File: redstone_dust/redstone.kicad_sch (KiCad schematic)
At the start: 72 parts, among them J1 1x4_Pogo, J2 1x4_Pogo, J3 1x4_Pogo, J4 1x4_Pogo, J5 1x4_Pogo, J6 1x4_Pogo, J7 1x4_Pogo, J8 1x4_Pogo, J9 2.54mm_ProgrammingPin, Q1 BC108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

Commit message: add some symbol footprints
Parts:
- D1, D10, D11, D12, D13, D14, D15, D16, D2, D3, D4, D5, D6, D7, D8, D9: footprint (none) -> SamacSys_Parts:LEDC1608X115N
- J9: footprint (none) -> Connector_PinSocket_2.54mm:PinSocket_1x04_P2.54mm_Vertical
- R1, R10, R11, R12, R13, R14, R15, R16, R17, R18, R19, R2, R20, R21, R3, R4, R5, R6, R7, R8, R9: footprint (none) -> Resistor_THT:R_Axial_DIN0204_L3.6mm_D1.6mm_P5.08mm_Horizontal
- SW1: footprint (none) -> Button_Switch_THT:SW_TH_Tactile_Omron_B3F-100x
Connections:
- net GND: now also J9.4 (Pin_4); no longer J9.1 (Pin_1)
- net at J9.2 (Pin_2): now also U1.24 (SWCLK); no longer U1.25 (SWD)
- net at J9.3 (Pin_3): now also U1.25 (SWD); no longer U1.24 (SWCLK)
- net at SW1.2 (B), U1.26 (RUN): now also J9.1 (Pin_1); no longer J9.4 (Pin_4)
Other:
- moved on the sheet: J9
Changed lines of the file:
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@@
 	)
 	(no_connect
-		(at 41.91 144.78)
+		(at 41.91 162.56)
 	)
 	(no_connect
@@
 			(width 0)
 			(type default)
+			(color 0 0 0 1)
 		)
 	)
@@
 			(width 0)
 			(type default)
+			(color 0 0 0 1)
 		)
 	)
@@
 	(wire
 		(pts
-			(xy 31.75 173.99) (xy 31.75 21.59)
+			(xy 22.86 173.99) (xy 22.86 21.59)
 		)
 		(stroke
@@
 	(wire
 		(pts
-			(xy 31.75 21.59) (xy 82.55 21.59)
+			(xy 22.86 21.59) (xy 82.55 21.59)
 		)
 		(stroke
@@
 	(wire
 		(pts
-			(xy 31.75 173.99) (xy 62.23 173.99)
+			(xy 22.86 173.99) (xy 62.23 173.99)
 		)
 		(stroke
@@
 			(width 0)
 			(type default)
+			(color 0 0 0 1)
 		)
 	)
@@
 			)
 		)
-		(property "Footprint" ""
+		(property "Footprint" "Resistor_THT:R_Axial_DIN0204_L3.6mm_D1.6mm_P5.08mm_Horizontal"
 			(at 207.01 35.56 0)
 			(effects
@@
 	(symbol
 		(lib_id "Connector_Generic_MountingPin:Conn_01x04_MountingPin")
-		(at 41.91 154.94 180)
+		(at 41.91 152.4 0)
+		(mirror y)
 		(unit 1)
 		(exclude_from_sim no)
@@
 		(on_board yes)
 		(dnp no)
-		(fields_autoplaced yes)
 		(property "Reference" "J9"
-			(at 39.37 152.0443 0)
+			(at 39.37 155.2957 0)
 			(effects
 				(font
@@
 		)
 		(property "Value" "2.54mm_ProgrammingPin"
-			(at 39.37 154.5843 0)
+			(at 39.37 152.7557 0)
 			(effects
 				(font
@@
 			)
 		)
-		(property "Footprint" ""
-			(at 41.91 154.94 0)
+		(property "Footprint" "Connector_PinSocket_2.54mm:PinSocket_1x04_P2.54mm_Vertical"
+			(at 41.91 152.4 0)
 			(effects
 				(font
@@
 		)
 		(property "Datasheet" "~"
-			(at 41.91 154.94 0)
+			(at 41.91 152.4 0)
 			(effects
 				(font
@@
 		)
 		(property "Description" "Generic connectable mounting pin connector, single row, 01x04, script generated (kicad-library-utils/schlib/autogen/connector/)"
-			(at 41.91 154.94 0)
+			(at 41.91 152.4 0)
 			(effects
 				(font
@@
 			)
 		)
-		(property "Footprint" ""
+		(property "Footprint" "SamacSys_Parts:LEDC1608X115N"
 			(at 207.01 25.4 0)
 			(effects
@@
 			)
 		)
-		(property "Footprint" ""
+		(property "Footprint" "Resistor_THT:R_Axial_DIN0204_L3.6mm_D1.6mm_P5.08mm_Horizontal"
 			(at 168.91 50.8 0)
 			(effects
@@
 			)
 		)
-		(property "Footprint" ""
+		(property "Footprint" "Resistor_THT:R_Axial_DIN0204_L3.6mm_D1.6mm_P5.08mm_Horizontal"
 			(at 217.17 52.07 0)
 			(effects
@@
 			)
 		)
-		(property "Footprint" ""
+		(property "Footprint" "SamacSys_Parts:LEDC1608X115N"
 			(at 196.85 25.4 0)
 			(effects
@@
 			)
 		)
-		(property "Footprint" ""
+		(property "Footprint" "Resistor_THT:R_Axial_DIN0204_L3.6mm_D1.6mm_P5.08mm_Horizontal"
 			(at 217.17 19.05 0)
 			(effects
@@
 			)
 		)
-		(property "Footprint" ""
+		(property "Footprint" "Resistor_THT:R_Axial_DIN0204_L3.6mm_D1.6mm_P5.08mm_Horizontal"
 			(at 207.01 19.05 0)
 			(effects
@@
 			)
 		)
-		(property "Footprint" ""
+		(property "Footprint" "Resistor_THT:R_Axial_DIN0204_L3.6mm_D1.6mm_P5.08mm_Horizontal"
 			(at 196.85 52.07 0)
 			(effects
@@
 			)
 		)
-		(property "Footprint" ""
+		(property "Footprint" "Resistor_THT:R_Axial_DIN0204_L3.6mm_D1.6mm_P5.08mm_Horizontal"
 			(at 171.45 62.23 0)
 			(effects
@@
 			)
 		)
-		(property "Footprint" ""
+		(property "Footprint" "Resistor_THT:R_Axial_DIN0204_L3.6mm_D1.6mm_P5.08mm_Horizontal"
 			(at 164.338 21.59 90)
 			(effects
@@
 			)
 		)
-		(property "Footprint" ""
+		(property "Footprint" "Resistor_THT:R_Axial_DIN0204_L3.6mm_D1.6mm_P5.08mm_Horizontal"
 			(at 196.85 68.58 0)
 			(effects
@@
 			)
 		)
-		(property "Footprint" ""
+		(property "Footprint" "SamacSys_Parts:LEDC1608X115N"
 			(at 196.85 41.91 0)
 			(effects
@@
 			)
 		)
-		(property "Footprint" ""
+		(property "Footprint" "SamacSys_Parts:LEDC1608X115N"
 			(at 186.69 41.91 0)
 			(effects
@@
 			)
 		)
-		(property "Footprint" ""
+		(property "Footprint" "SamacSys_Parts:LEDC1608X115N"
 			(at 207.01 74.93 0)
 			(effects
@@
 			)
 		)
-		(property "Footprint" ""
+		(property "Footprint" "Resistor_THT:R_Axial_DIN0204_L3.6mm_D1.6mm_P5.08mm_Horizontal"
 			(at 217.17 35.56 0)
 			(effects
@@
 			)
 		)
-		(property "Footprint" ""
+		(property "Footprint" "SamacSys_Parts:LEDC1608X115N"
 			(at 186.69 25.4 0)
 			(effects
@@
 			)
 		)
-		(property "Footprint" ""
+		(property "Footprint" "SamacSys_Parts:LEDC1608X115N"
 			(at 207.01 41.91 0)
 			(effects
@@
 			)
 		)
-		(property "Footprint" ""
+		(property "Footprint" "SamacSys_Parts:LEDC1608X115N"
 			(at 217.17 25.4 0)
 			(effects
@@
 			)
 		)
-		(property "Footprint" ""
+		(property "Footprint" "Resistor_THT:R_Axial_DIN0204_L3.6mm_D1.6mm_P5.08mm_Horizontal"
 			(at 196.85 35.56 0)
 			(effects
@@
 			)
 		)
-		(property "Footprint" ""
+		(property "Footprint" "SamacSys_Parts:LEDC1608X115N"
 			(at 186.69 74.93 0)
 			(effects
@@
 			)
 		)
-		(property "Footprint" ""
+		(property "Footprint" "SamacSys_Parts:LEDC1608X115N"
 			(at 186.69 58.42 0)
 			(effects
@@
 			)
 		)
-		(property "Footprint" ""
+		(property "Footprint" "Resistor_THT:R_Axial_DIN0204_L3.6mm_D1.6mm_P5.08mm_Horizontal"
 			(at 173.99 77.47 0)
 			(effects
@@
 			)
 		)
-		(property "Footprint" ""
+		(property "Footprint" "SamacSys_Parts:LEDC1608X115N"
 			(at 217.17 58.42 0)
 			(effects
@@
 			)
 		)
-		(property "Footprint" ""
+		(property "Footprint" "SamacSys_Parts:LEDC1608X115N"
 			(at 207.01 58.42 0)
 			(effects
@@
 			)
 		)
-		(property "Footprint" ""
+		(property "Footprint" "SamacSys_Parts:LEDC1608X115N"
 			(at 196.85 74.93 0)
 			(effects
@@
 			)
 		)
-		(property "Footprint" ""
+		(property "Footprint" "SamacSys_Parts:LEDC1608X115N"
 			(at 217.17 74.93 0)
 			(effects
@@
 			)
 		)
-		(property "Footprint" ""
+		(property "Footprint" "Resistor_THT:R_Axial_DIN0204_L3.6mm_D1.6mm_P5.08mm_Horizontal"
 			(at 196.85 19.05 0)
 			(effects
@@
 			)
 		)
-		(property "Footprint" ""
+		(property "Footprint" "Resistor_THT:R_Axial_DIN0204_L3.6mm_D1.6mm_P5.08mm_Horizontal"
 			(at 186.69 68.58 0)
 			(effects
@@
 			)
 		)
-		(property "Footprint" ""
+		(property "Footprint" "Resistor_THT:R_Axial_DIN0204_L3.6mm_D1.6mm_P5.08mm_Horizontal"
 			(at 181.61 90.17 0)
 			(effects
@@
 			)
 		)
-		(property "Footprint" ""
+		(property "Footprint" "Resistor_THT:R_Axial_DIN0204_L3.6mm_D1.6mm_P5.08mm_Horizontal"
 			(at 186.69 35.56 0)
 			(effects
@@
 			)
 		)
-		(property "Footprint" ""
+		(property "Footprint" "SamacSys_Parts:LEDC1608X115N"
 			(at 217.17 41.91 0)
 			(effects
@@
 			)
 		)
-		(property "Footprint" ""
+		(property "Footprint" "Resistor_THT:R_Axial_DIN0204_L3.6mm_D1.6mm_P5.08mm_Horizontal"
 			(at 207.01 52.07 0)
 			(effects
@@
 			)
 		)
-		(property "Footprint" ""
+		(property "Footprint" "Resistor_THT:R_Axial_DIN0204_L3.6mm_D1.6mm_P5.08mm_Horizontal"
 			(at 186.69 52.07 0)
 			(effects
@@
 			)
 		)
-		(property "Footprint" ""
+		(property "Footprint" "Resistor_THT:R_Axial_DIN0204_L3.6mm_D1.6mm_P5.08mm_Horizontal"
 			(at 207.01 68.58 0)
 			(effects
@@
 			)
 		)
-		(property "Footprint" ""
+		(property "Footprint" "Resistor_THT:R_Axial_DIN0204_L3.6mm_D1.6mm_P5.08mm_Horizontal"
 			(at 217.17 68.58 0)
 			(effects
@@
 			)
 		)
-		(property "Footprint" ""
+		(property "Footprint" "Resistor_THT:R_Axial_DIN0204_L3.6mm_D1.6mm_P5.08mm_Horizontal"
 			(at 186.69 19.05 0)
 			(effects
@@
 			)
 		)
-		(property "Footprint" ""
+		(property "Footprint" "SamacSys_Parts:LEDC1608X115N"
 			(at 196.85 58.42 0)
 			(effects
@@
 			)
 		)
-		(property "Footprint" ""
+		(property "Footprint" "Button_Switch_THT:SW_TH_Tactile_Omron_B3F-100x"
 			(at 53.34 62.23 0)
 			(effects

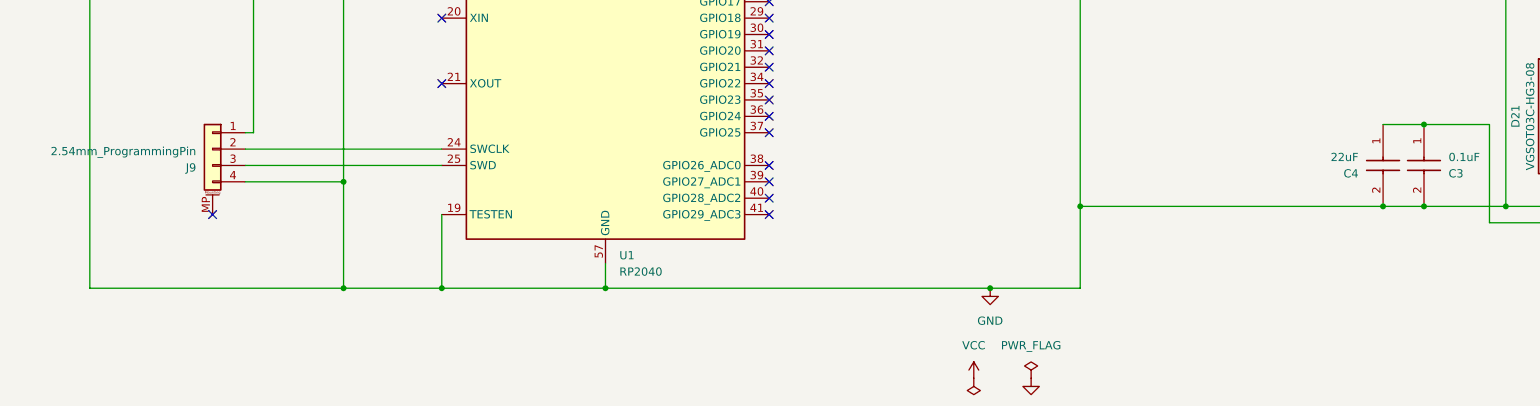
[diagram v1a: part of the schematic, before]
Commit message: add footprint for pogo pins
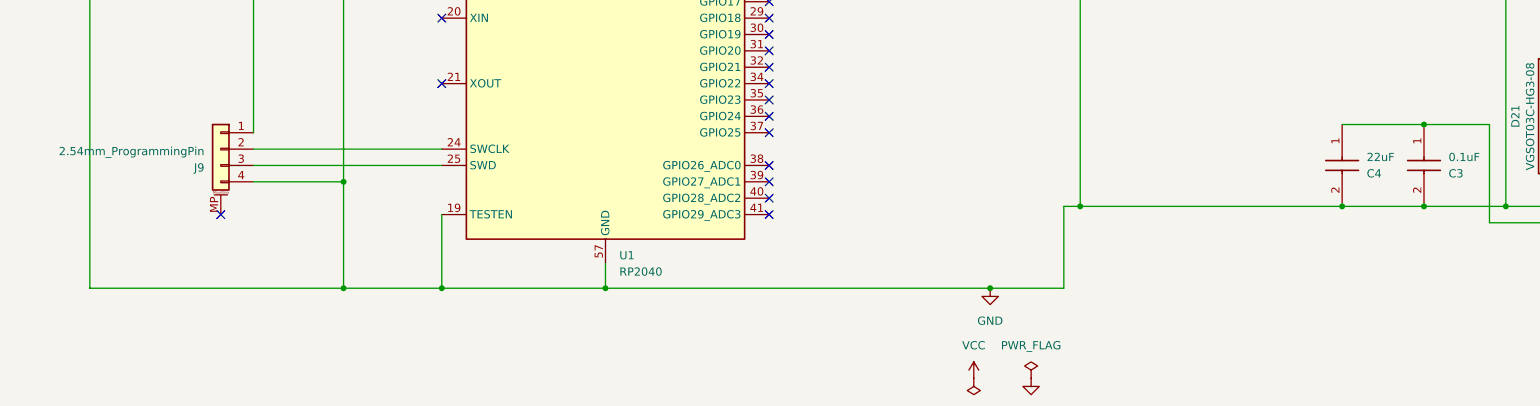
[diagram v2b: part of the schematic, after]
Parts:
- J1, J2, J3, J4, J5, J6, J7, J8: footprint (none) -> Connector_PinSocket_2.54mm:PinSocket_1x04_P2.54mm_Vertical
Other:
- moved on the sheet: C4, J9
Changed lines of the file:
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@@
 	)
 	(junction
-		(at 223.52 161.29)
-		(diameter 0)
-		(color 0 0 0 1)
-	)
-	(junction
 		(at 262.89 21.59)
 		(diameter 0)
@@
 	)
 	(junction
+		(at 217.17 161.29)
+		(diameter 0)
+		(color 0 0 0 0)
+	)
+	(junction
 		(at 260.35 62.23)
 		(diameter 0)
@@
 	)
 	(no_connect
-		(at 41.91 162.56)
+		(at 43.18 162.56)
 	)
 	(no_connect
@@
 	(wire
 		(pts
+			(xy 217.17 161.29) (xy 229.87 161.29)
+		)
+		(stroke
+			(width 0)
+			(type default)
+			(color 0 0 0 1)
+		)
+	)
+	(wire
+		(pts
 			(xy 260.35 118.11) (xy 260.35 128.27)
 		)
@@
 	(wire
 		(pts
-			(xy 46.99 154.94) (xy 77.47 154.94)
+			(xy 48.26 154.94) (xy 77.47 154.94)
 		)
 		(stroke
@@
 	(wire
 		(pts
-			(xy 46.99 149.86) (xy 48.26 149.86)
+			(xy 226.06 16.51) (xy 226.06 33.02)
 		)
 		(stroke
 			(width 0)
 			(type default)
+			(color 255 0 0 1)
 		)
 	)
 	(wire
 		(pts
-			(xy 226.06 16.51) (xy 226.06 33.02)
+			(xy 265.43 100.33) (xy 265.43 113.03)
 		)
 		(stroke
 			(width 0)
 			(type default)
-			(color 255 0 0 1)
+			(color 0 194 194 1)
 		)
 	)
 	(wire
 		(pts
-			(xy 265.43 100.33) (xy 265.43 113.03)
+			(xy 173.99 161.29) (xy 176.53 161.29)
 		)
 		(stroke
 			(width 0)
 			(type default)
-			(color 0 194 194 1)
+			(color 0 0 0 1)
 		)
 	)
@@
 	(wire
 		(pts
-			(xy 176.53 173.99) (xy 176.53 161.29)
+			(xy 173.99 173.99) (xy 173.99 161.29)
 		)
 		(stroke
@@
 	(wire
 		(pts
-			(xy 223.52 148.59) (xy 229.87 148.59)
-		)
-		(stroke
-			(width 0)
-			(type default)
-			(color 194 0 0 1)
-		)
-	)
-	(wire
-		(pts
 			(xy 176.53 63.5) (xy 176.53 80.01)
 		)
@@
 	(wire
 		(pts
-			(xy 176.53 161.29) (xy 223.52 161.29)
+			(xy 176.53 161.29) (xy 217.17 161.29)
 		)
 		(stroke
@@
 	(wire
 		(pts
-			(xy 46.99 152.4) (xy 77.47 152.4)
+			(xy 48.26 152.4) (xy 77.47 152.4)
 		)
 		(stroke
@@
 	(wire
 		(pts
-			(xy 223.52 161.29) (xy 229.87 161.29)
-		)
-		(stroke
-			(width 0)
-			(type default)
-			(color 0 0 0 1)
-		)
-	)
-	(wire
-		(pts
 			(xy 72.39 109.22) (xy 77.47 109.22)
 		)
@@
 	(wire
 		(pts
-			(xy 162.56 173.99) (xy 176.53 173.99)
+			(xy 162.56 173.99) (xy 173.99 173.99)
 		)
 		(stroke
@@
 	(wire
 		(pts
+			(xy 217.17 148.59) (xy 229.87 148.59)
+		)
+		(stroke
+			(width 0)
+			(type default)
+			(color 194 0 0 1)
+		)
+	)
+	(wire
+		(pts
 			(xy 162.56 25.4) (xy 162.56 36.83)
 		)
@@
 	(wire
 		(pts
-			(xy 46.99 157.48) (xy 62.23 157.48)
+			(xy 48.26 157.48) (xy 62.23 157.48)
 		)
 		(stroke
@@
 	(symbol
 		(lib_id "Connector_Generic_MountingPin:Conn_01x04_MountingPin")
-		(at 41.91 152.4 0)
+		(at 43.18 152.4 0)
 		(mirror y)
 		(unit 1)
@@
 		(dnp no)
 		(property "Reference" "J9"
-			(at 39.37 155.2957 0)
+			(at 40.64 155.2957 0)
 			(effects
 				(font
@@
 		)
 		(property "Value" "2.54mm_ProgrammingPin"
-			(at 39.37 152.7557 0)
+			(at 40.64 152.7557 0)
 			(effects
 				(font
@@
 		)
 		(property "Footprint" "Connector_PinSocket_2.54mm:PinSocket_1x04_P2.54mm_Vertical"
-			(at 41.91 152.4 0)
+			(at 43.18 152.4 0)
 			(effects
 				(font
@@
 		)
 		(property "Datasheet" "~"
-			(at 41.91 152.4 0)
+			(at 43.18 152.4 0)
 			(effects
 				(font
@@
 		)
 		(property "Description" "Generic connectable mounting pin connector, single row, 01x04, script generated (kicad-library-utils/schlib/autogen/connector/)"
-			(at 41.91 152.4 0)
+			(at 43.18 152.4 0)
 			(effects
 				(font
@@
 	(symbol
 		(lib_id "SamacSys_Parts:GRM188C81A226ME01D")
-		(at 223.52 148.59 270)
+		(at 217.17 148.59 90)
+		(mirror x)
 		(unit 1)
 		(exclude_from_sim no)
@@
 		(dnp no)
 		(property "Reference" "C4"
-			(at 219.71 156.2101 90)
+			(at 220.98 156.2101 90)
 			(effects
 				(font
@@
 		)
 		(property "Value" "22uF"
-			(at 219.71 153.6701 90)
+			(at 220.98 153.6701 90)
 			(effects
 				(font
@@
 		)
 		(property "Footprint" "GRM18x"
-			(at 127.33 157.48 0)
+			(at 313.36 157.48 0)
 			(effects
 				(font
@@
 		)
 		(property "Datasheet" "https://search.murata.co.jp/Ceramy/image/img/A01X/G101/ENG/GRM188C81A226ME01-01A.pdf"
-			(at 27.33 157.48 0)
+			(at 413.36 157.48 0)
 			(effects
 				(font
@@
 		)
 		(property "Description" "MLCC, 0603"
-			(at 223.52 148.59 0)
+			(at 217.17 148.59 0)
 			(effects
 				(font
@@
 		)
 		(property "Height" "0.9"
-			(at -172.67 157.48 0)
+			(at 613.36 157.48 0)
 			(effects
 				(font
@@
 		)
 		(property "Manufacturer_Name" "Murata Electronics"
-			(at -272.67 157.48 0)
+			(at 713.36 157.48 0)
 			(effects
 				(font
@@
 		)
 		(property "Manufacturer_Part_Number" "GRM188C81A226ME01D"
-			(at -372.67 157.48 0)
+			(at 813.36 157.48 0)
 			(effects
 				(font
@@
 		)
 		(property "Mouser Part Number" ""
-			(at -472.67 157.48 0)
+			(at 913.36 157.48 0)
 			(effects
 				(font
@@
 		)
 		(property "Mouser Price/Stock" ""
-			(at -572.67 157.48 0)
+			(at 1013.36 157.48 0)
 			(effects
 				(font
@@
 		)
 		(property "Arrow Part Number" ""
-			(at -672.67 157.48 0)
+			(at 1113.36 157.48 0)
 			(effects
 				(font
@@
 		)
 		(property "Arrow Price/Stock" ""
-			(at -772.67 157.48 0)
+			(at 1213.36 157.48 0)
 			(effects
 				(font
@@
 			)
 		)
-		(property "Footprint" ""
+		(property "Footprint" "Connector_PinSocket_2.54mm:PinSocket_1x04_P2.54mm_Vertical"
 			(at 270.51 151.13 0)
 			(effects
@@
 			)
 		)
-		(property "Footprint" ""
+		(property "Footprint" "Connector_PinSocket_2.54mm:PinSocket_1x04_P2.54mm_Vertical"
 			(at 270.51 95.25 0)
 			(effects
@@
 			)
 		)
-		(property "Footprint" ""
+		(property "Footprint" "Connector_PinSocket_2.54mm:PinSocket_1x04_P2.54mm_Vertical"
 			(at 270.51 85.09 0)
 			(effects
@@
 			)
 		)
-		(property "Footprint" ""
+		(property "Footprint" "Connector_PinSocket_2.54mm:PinSocket_1x04_P2.54mm_Vertical"
 			(at 270.51 52.07 0)
 			(effects
@@
 			)
 		)
-		(property "Footprint" ""
+		(property "Footprint" "Connector_PinSocket_2.54mm:PinSocket_1x04_P2.54mm_Vertical"
 			(at 270.51 29.21 0)
 			(effects
@@
 			)
 		)
-		(property "Footprint" ""
+		(property "Footprint" "Connector_PinSocket_2.54mm:PinSocket_1x04_P2.54mm_Vertical"
 			(at 270.51 62.23 0)
 			(effects
@@
 			)
 		)
-		(property "Footprint" ""
+		(property "Footprint" "Connector_PinSocket_2.54mm:PinSocket_1x04_P2.54mm_Vertical"
 			(at 270.51 118.11 0)
 			(effects
@@
 			)
 		)
-		(property "Footprint" ""
+		(property "Footprint" "Connector_PinSocket_2.54mm:PinSocket_1x04_P2.54mm_Vertical"
 			(at 270.51 128.27 0)
 			(effects

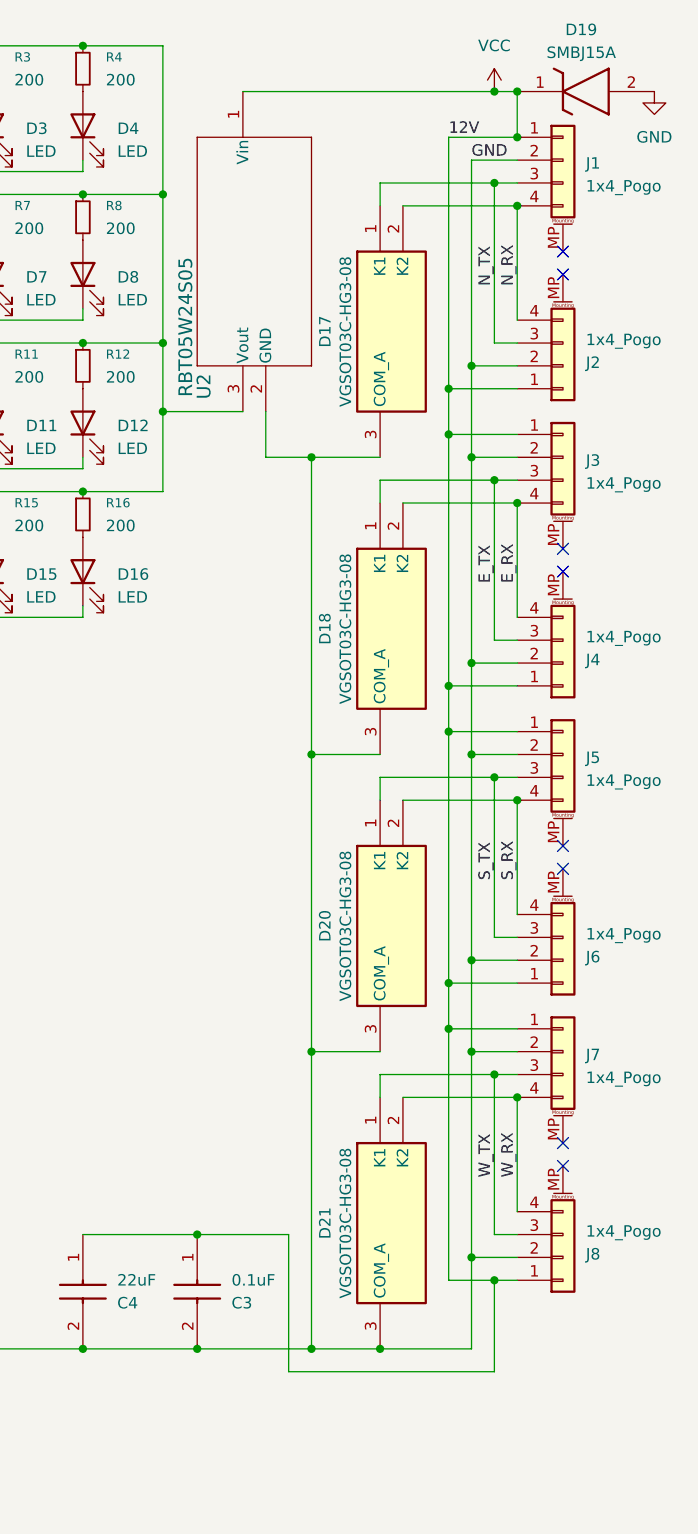
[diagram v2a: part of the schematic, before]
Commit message: switch GND and VCC pins to match pcb footprint
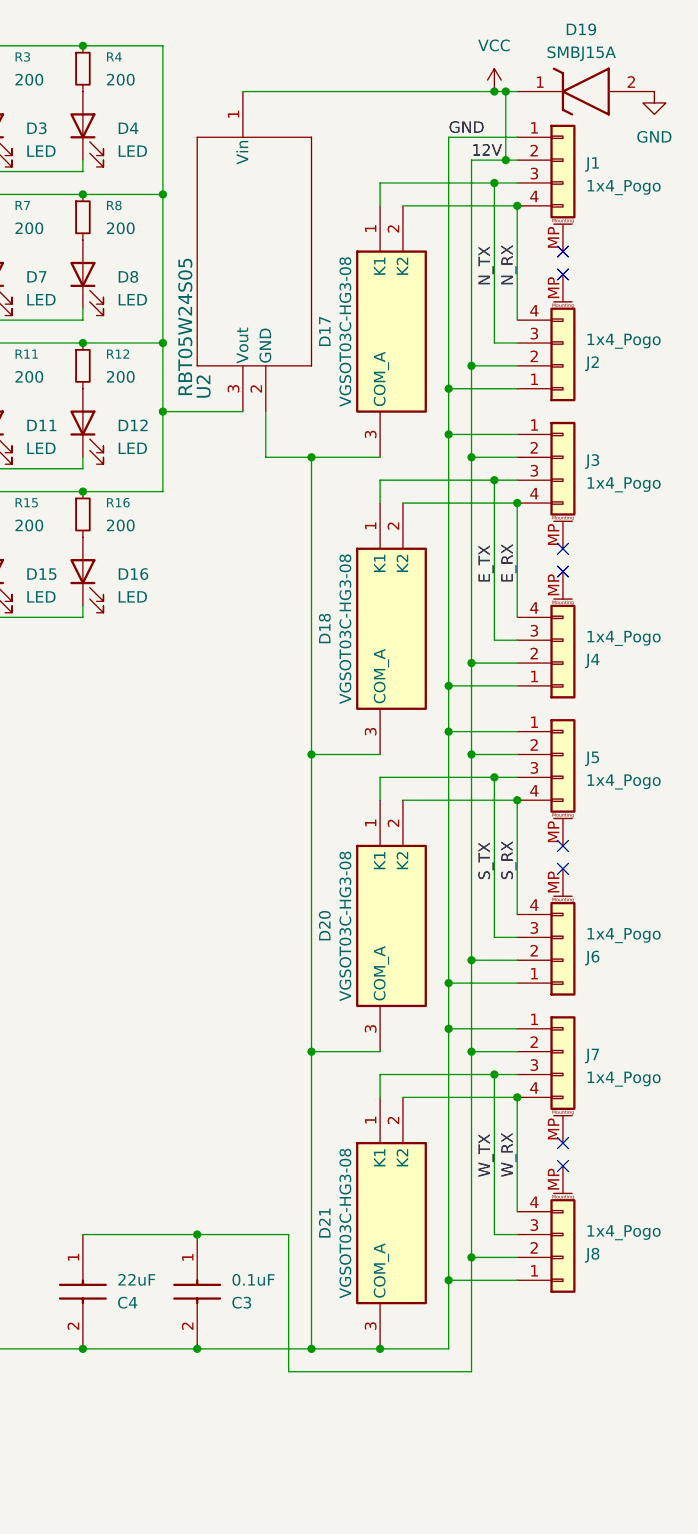
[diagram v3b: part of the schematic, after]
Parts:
- R1, R10, R11, R12, R13, R14, R15, R16, R2, R3, R4, R5, R6, R7, R8, R9: footprint Resistor_THT:R_Axial_DIN0204_L3.6mm_D1.6mm_P5.08mm_Horizontal -> SamacSys_Parts:CRCW1210200RJNEAIF
- R17: footprint Resistor_THT:R_Axial_DIN0204_L3.6mm_D1.6mm_P5.08mm_Horizontal -> SamacSys_Parts:TNPW0805100KFHEA
- R18, R19, R20, R21: footprint Resistor_THT:R_Axial_DIN0204_L3.6mm_D1.6mm_P5.08mm_Horizontal -> SamacSys_Parts:ERJ-UP6D1001V
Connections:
- net GND: now also J1.1 (Pin_1), J2.1 (Pin_1), J3.1 (Pin_1), J4.1 (Pin_1), J5.1 (Pin_1), J6.1 (Pin_1), J7.1 (Pin_1), J8.1 (Pin_1); no longer J1.2 (Pin_2), J2.2 (Pin_2), J3.2 (Pin_2), J4.2 (Pin_2), J5.2 (Pin_2), J6.2 (Pin_2), J7.2 (Pin_2), J8.2 (Pin_2)
- net VCC: now also J1.2 (Pin_2), J2.2 (Pin_2), J3.2 (Pin_2), J4.2 (Pin_2), J5.2 (Pin_2), J6.2 (Pin_2), J7.2 (Pin_2), J8.2 (Pin_2); no longer J1.1 (Pin_1), J2.1 (Pin_1), J3.1 (Pin_1), J4.1 (Pin_1), J5.1 (Pin_1), J6.1 (Pin_1), J7.1 (Pin_1), J8.1 (Pin_1)
